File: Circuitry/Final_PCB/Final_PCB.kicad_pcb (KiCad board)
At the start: 2 copper layers, 182.6 x 75.3 mm, 88 parts, among them Q1 Q_NMOS_GDS, Q10 Q_NMOS_GDS, Q11 Q_NMOS_GDS, Q12 Q_NMOS_GDS, Q13 Q_NMOS_GDS, Q14 Q_NMOS_GDS, Q15 Q_NMOS_GDS, Q16 Q_NMOS_GDS, Q2 Q_NMOS_GDS, Q3 Q_NMOS_GDS, Q4 Q_NMOS_GDS, Q5 Q_NMOS_GDS, Q6 Q_NMOS_GDS, Q7 Q_NMOS_GDS, Q8 Q_NMOS_GDS, Q9 Q_NMOS_GDS

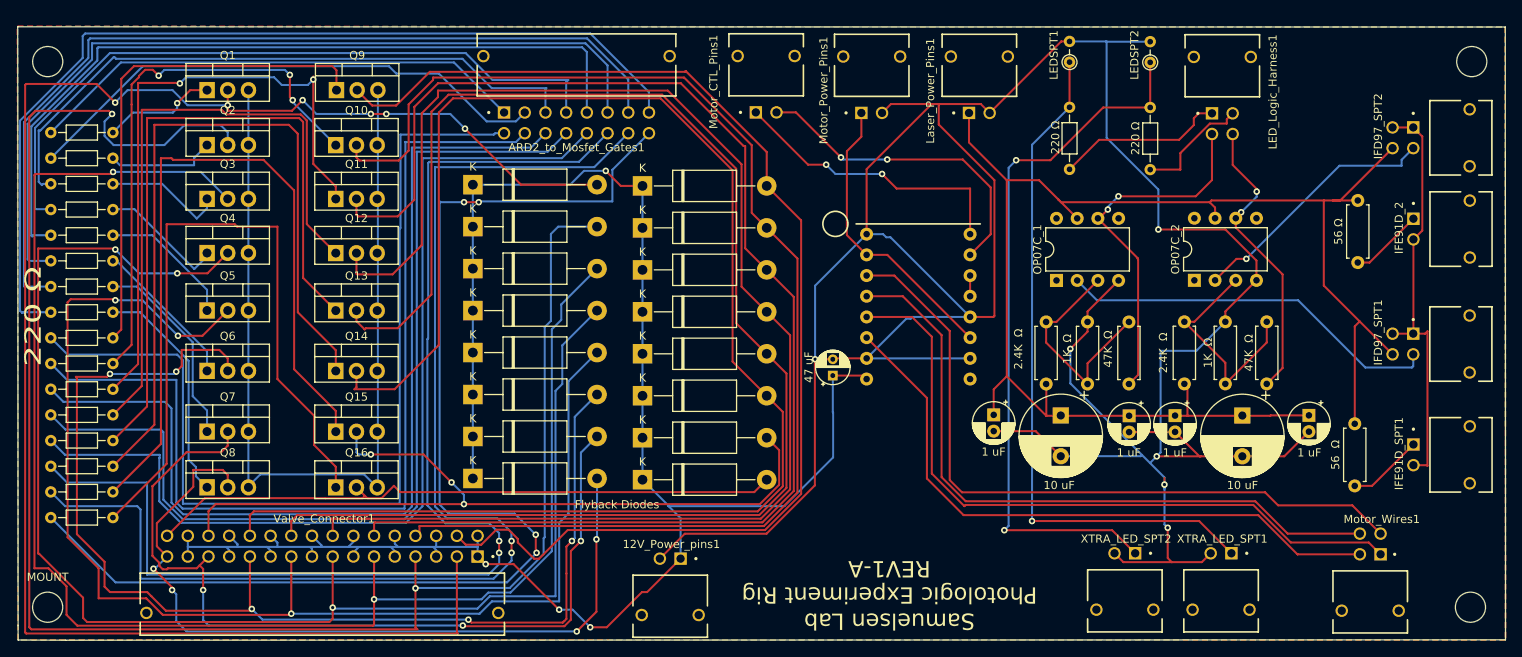
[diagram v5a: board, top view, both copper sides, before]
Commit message: add new mainboard design, led breakout board design kicad
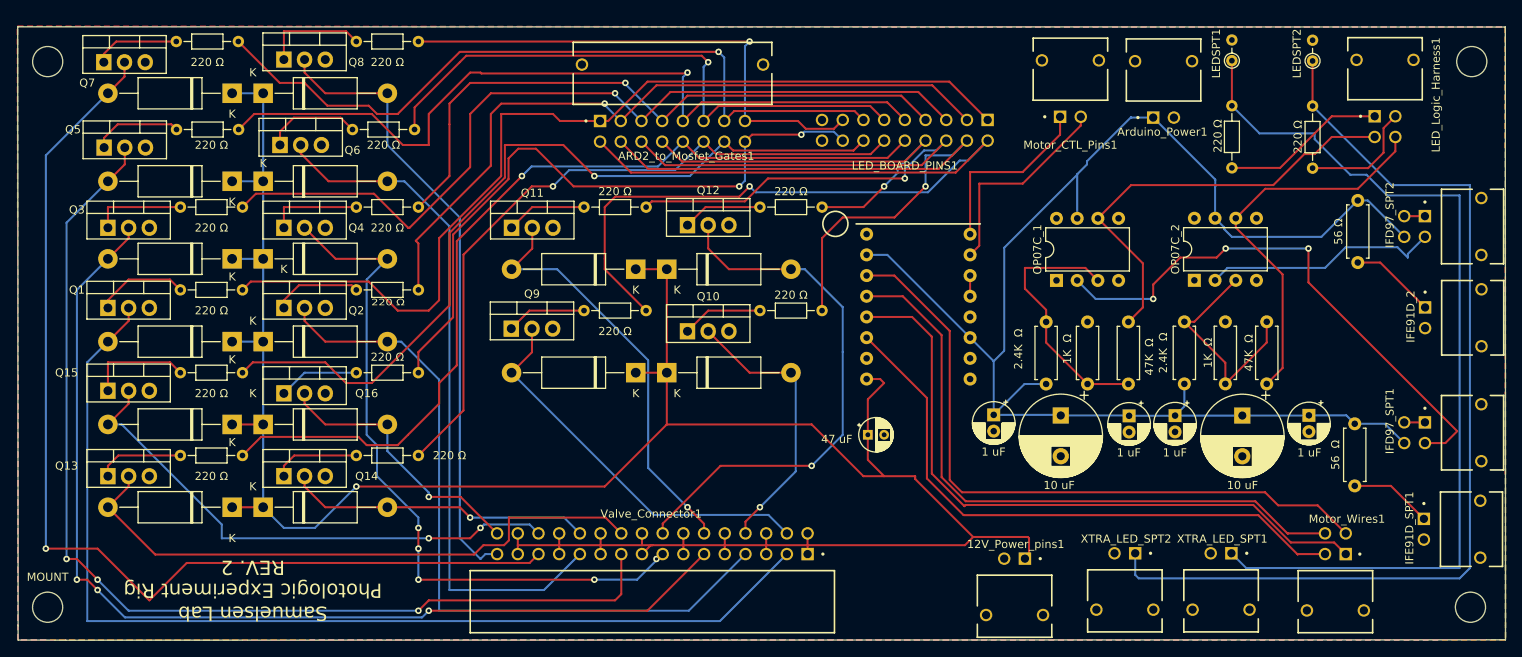
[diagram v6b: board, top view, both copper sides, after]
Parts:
- removed Laser_Power_Pins1: IPL1-102-01-L-S-RE1-K-WT, Samtech Components:SAMTEC_IPL1-102-01-L-S-RE1-K-WT
- added LED_BOARD_PINS1: IPL1-108-01-L-D-RE1-K-WT, IPL1-109-01-L-D-RE1-K:SAMTEC_IPL1-109-01-L-D-RE1-K, B.Cu at (186.7, 79.5)
- 12V_Power_pins1, IFE91D_2, IFE91D_SPT1, Motor_CTL_Pins1, XTRA_LED_SPT1, XTRA_LED_SPT2: footprint Samtech Components:SAMTEC_IPL1-102-01-L-S-RE1-K-WT -> IPL1-102-01-L-S-RE1-K-WT:SAMTEC_IPL1-102-01-L-S-RE1-K-WT
- ARD2_to_Mosfet_Gates1: footprint Samtech Components:SAMTEC_IPL1-108-01-L-D-RE1-K-WT -> IPL1-108-01-L-D-RE1-K-WT:SAMTEC_IPL1-108-01-L-D-RE1-K-WT
- Arduino_Power1: renamed from Motor_Power_Pins1; footprint Samtech Components:SAMTEC_IPL1-102-01-L-S-RE1-K-WT -> IPL1-102-01-L-S-RE1-K-WT:SAMTEC_IPL1-102-01-L-S-RE1-K-WT
- IFD97_SPT1, IFD97_SPT2, LED_Logic_Harness1, Motor_Wires1: footprint Samtech Components:SAMTEC_IPL1-102-01-X-D-RE1-K-WT -> IPL1-102-01-L-D-RE1-K-WT:SAMTEC_IPL1-102-01-L-D-RE1-K-WT
- Valve_Connector1: footprint Samtech Components:SAMTEC_IPL1-116-01-X-D-RE1-K-WT -> IPL1-116-01-X-D-RE1-K:SAMTEC_IPL1-116-01-X-D-RE1-K
- moved R20 98.0 mm to (176.5, 88.9), turned to 180 degrees
- moved R18 94.9 mm to (176.5, 101.6), turned to 180 degrees
- moved R19 76.4 mm to (154.9, 88.9), turned to 180 degrees
- moved R17 73.1 mm to (154.9, 101.6), turned to 180 degrees
- moved R16 56.0 mm to (127.0, 68.6), turned to 180 degrees
- moved D8 53.8 mm to (108.0, 74.9)
- moved D13 53.8 mm to (104.1, 125.7), turned to 180 degrees
- moved Q8 53.3 mm to (110.5, 70.8)
- moved D7 51.4 mm to (104.1, 74.9), turned to 180 degrees
- moved D15 50.4 mm to (104.1, 115.6), turned to 180 degrees
- moved Q10 48.8 mm to (160.0, 104.1)
- moved D14 48.5 mm to (108.0, 125.7)
- moved R24 48.5 mm to (127.0, 109.2), turned to 180 degrees
- moved R10 47.9 mm to (127.0, 99.1), turned to 180 degrees
- moved R14 47.5 mm to (126.5, 79.4), turned to 180 degrees
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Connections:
- net /12V_GND renamed /GND
- net /R1_P3 renamed /side_one_pin_3
- net /R5_P3 renamed /side_two_pin_three
- Arduino_Power1 pad 01: /5V_ARD2 -> /5V_ARD
- C1 pad 1: /5V_ARD1 -> /5V_ARD
- C2 pad 1: /5V_ARD1 -> /5V_ARD
- C3 pad 1: /5V_ARD1 -> /5V_ARD
- C4 pad 1: /5V_ARD1 -> /5V_ARD
- C5 pad 1: /5V_ARD1 -> /5V_ARD
- C6 pad 1: /5V_ARD1 -> /5V_ARD
- IFD97_SPT1 pad 04: /5V_ARD1 -> /5V_ARD
- IFD97_SPT2 pad 04: /5V_ARD1 -> /5V_ARD
- MOTOR_DRIVER1 pad 11: /5V_ARD2 -> /5V_ARD
- MOTOR_DRIVER1 pad 2: /5V_ARD2 -> /5V_ARD
- OP07C_1 pad 7: /5V_ARD1 -> /5V_ARD
- OP07C_2 pad 7: /5V_ARD1 -> /5V_ARD
- R1 pad 1: /5V_ARD1 -> /5V_ARD
- R4 pad 1: /5V_ARD1 -> /5V_ARD
- R5 pad 1: /5V_ARD1 -> /5V_ARD
- R8 pad 1: /5V_ARD1 -> /5V_ARD
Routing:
- net /GND: track 539.6 -> 5.08 mm, vias 6 -> 0
- net /5V_ARD1: track 181.7 -> 0.00 mm
- net /5V_ARD: track 0.00 -> 181.2 mm
- net /V14 GND: track 194.6 -> 37.4 mm, vias 0 -> 1
- net /V2 GND: track 214.8 -> 89.9 mm, vias 2 -> 0
- net /V10 GND: track 155.8 -> 34.8 mm, vias 0 -> 1
- net /V11 GND: track 165.9 -> 51.6 mm, vias 0 -> 1
- net /V12 GND: track 175.2 -> 65.8 mm, vias 0 -> 1
- net /V13 GND: track 183.1 -> 74.6 mm
- net /V9 GND: track 149.1 -> 48.4 mm
- net /V4 GND: track 177.1 -> 86.1 mm, vias 3 -> 5
- net Net-(Q14-G): track 93.1 -> 10.7 mm
- net Net-(Q15-G): track 93.1 -> 12.9 mm
- net /V1 GND: track 209.8 -> 129.8 mm, vias 6 -> 0
- net Net-(Q16-G): track 87.4 -> 9.94 mm
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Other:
- board text added: "Samuelsen Lab Photologic Experiment Rig REV. 2"
- board text removed: "Flyback Diodes"
- board text removed: "Samuelsen Lab Photologic Experiment Rig REV1-A"
